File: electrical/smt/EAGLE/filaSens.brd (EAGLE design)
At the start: 50 x 20 mm, 16 parts, among them IC2 SS495, IC3 TINY85

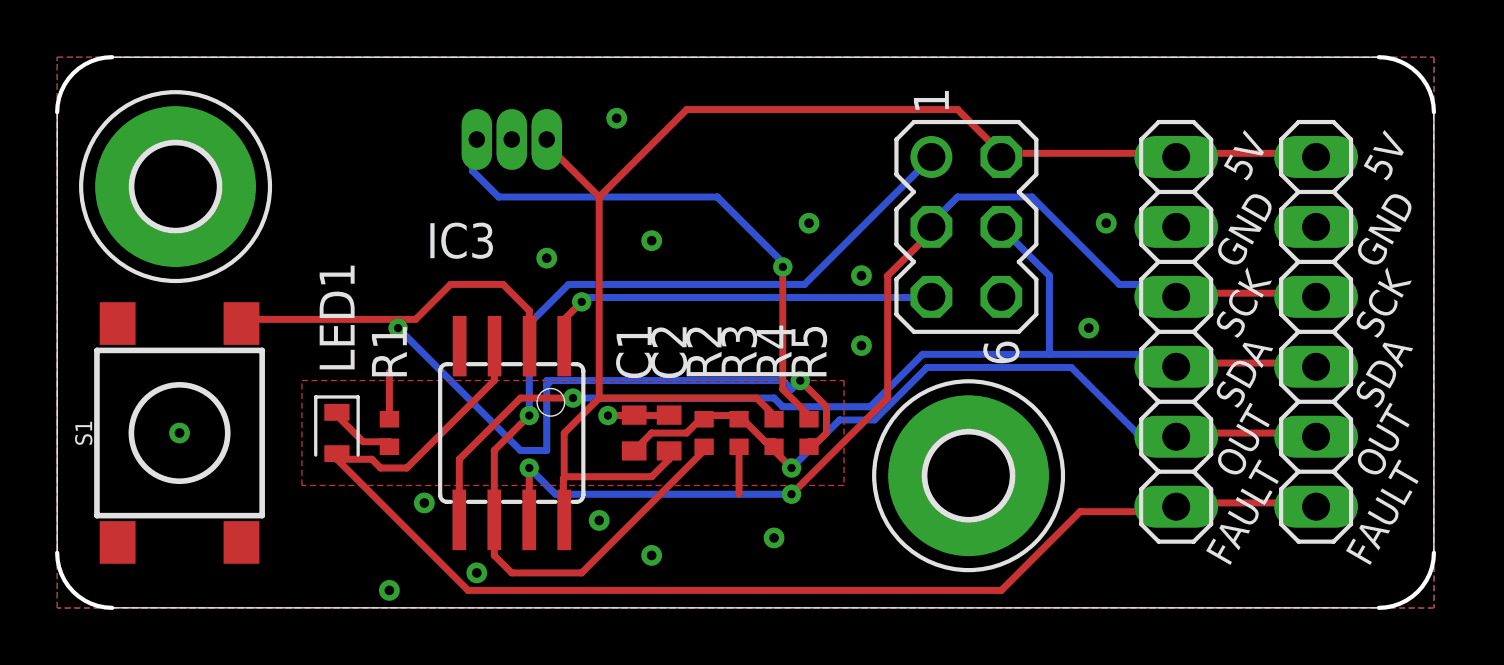
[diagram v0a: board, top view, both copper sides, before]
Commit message: change EAGLE files to capture PR #28 and Issue #27
change EAGLE files to capture PR #28 and Issue #27

Update GERBER files as well as EAGLE files
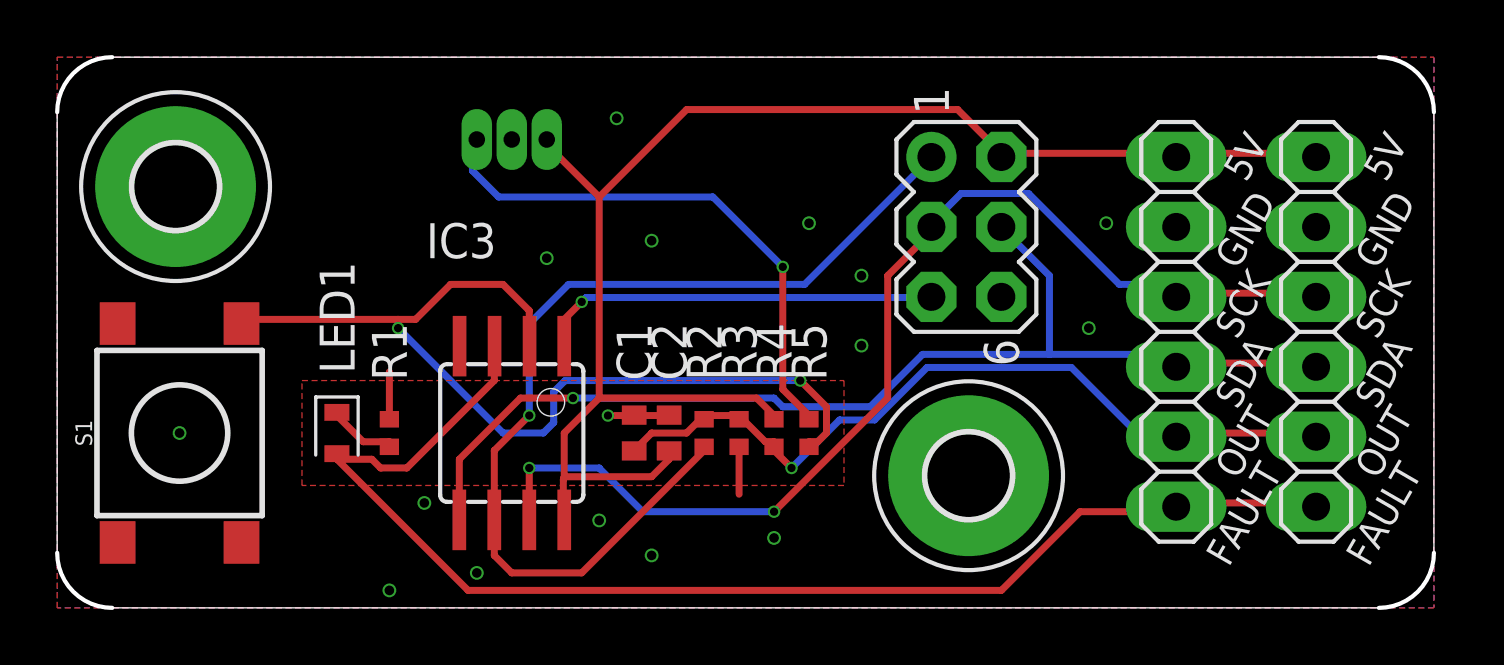
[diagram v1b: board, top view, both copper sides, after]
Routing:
- net IN: track 35.7 -> 33.9 mm
- net SCK: track 40.0 -> 40.6 mm

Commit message: Fixed cap gnd, made 5v trace larger, re-routed some traces to be cleaner
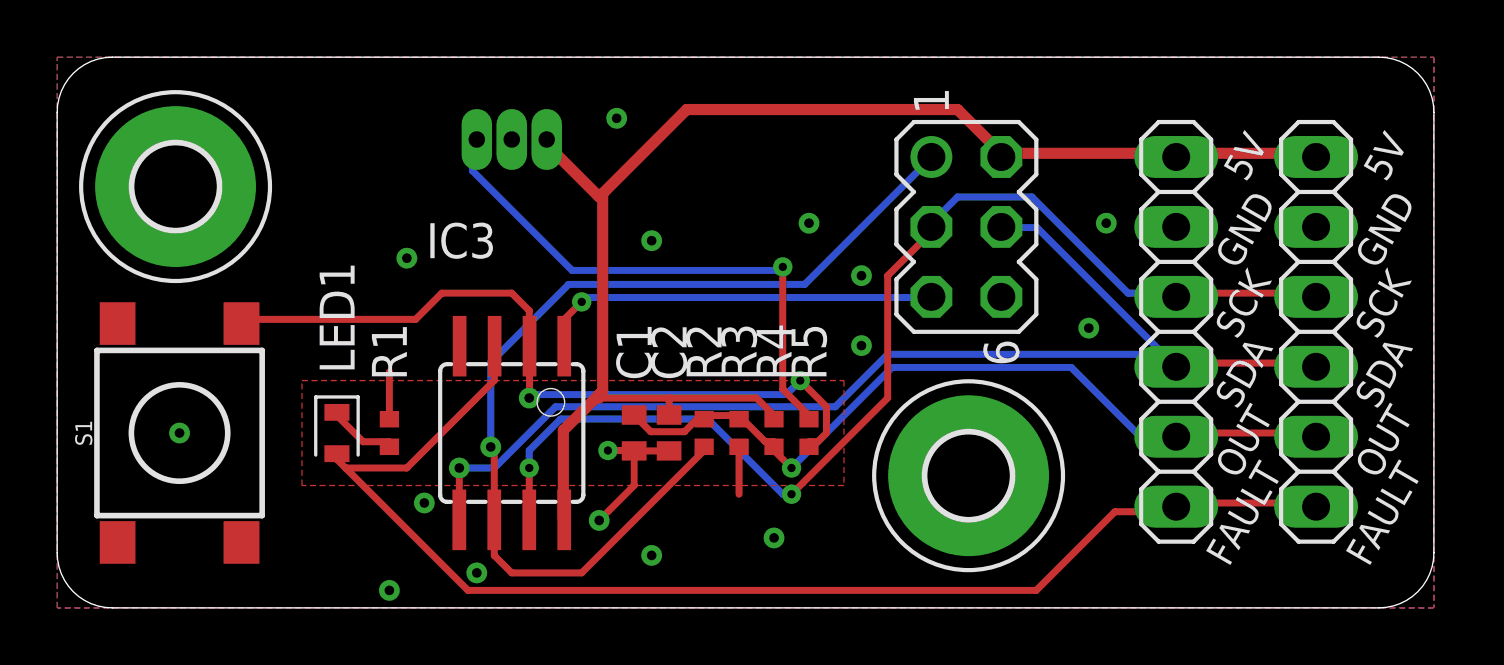
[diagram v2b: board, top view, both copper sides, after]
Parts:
- turned C1 to 270 degrees
- turned C2 to 270 degrees
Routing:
- net IN: track 33.9 -> 27.7 mm
- net +5V: track 54.7 -> 51.2 mm
- net GND: track 5.70 -> 8.72 mm
- net SDA: track 41.0 -> 43.7 mm
- net SCK: track 40.6 -> 41.8 mm
